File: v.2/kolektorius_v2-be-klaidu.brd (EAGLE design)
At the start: 100 x 50 mm, 81 parts, among them IC1 LM1117-33, IC2 ENC28J60, K1 G5V1, K2 G5V1, K3 G5V1, T1 2N2222, T2 2N2222, T3 2N2222, T4 2N2222, U1 ATMEGA328P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

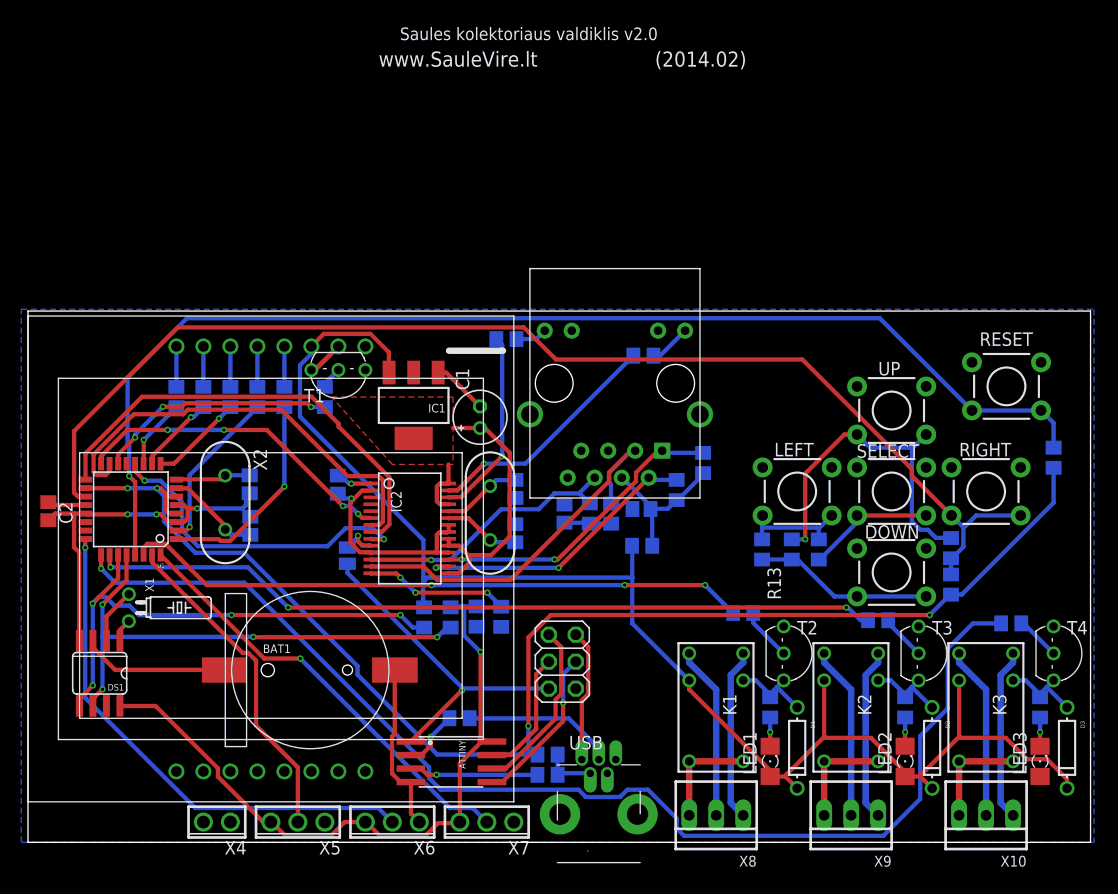
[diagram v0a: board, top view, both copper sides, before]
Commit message: prijungta prie tinklo emoncms
veikiantis pvz
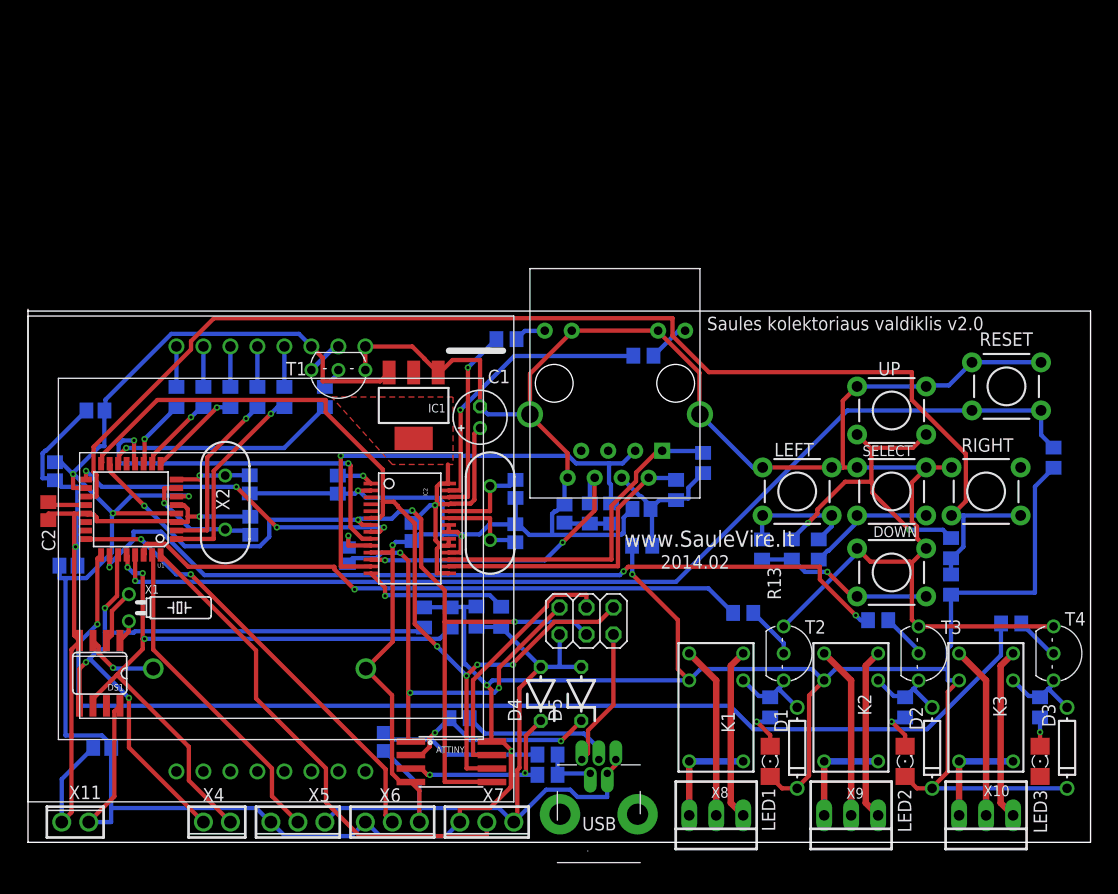
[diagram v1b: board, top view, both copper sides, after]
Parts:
- added C10, C11, C12, C14, C15, C16: 100n, resistor:C0805
- added D4, D5: (no value), diode:ZDIO-5
- added X11: (no value), con-phoenix-254:2POL254
- BAT1: device SparkFunNew:BATTCON_12MM_SMT -> SparkFun-Electromechanical:BATTCOM_20MM_PTH
- X2: value 25MHz -> 16MHz
- moved BAT1 9.23 mm to (31.8, 16.3), flipped to the bottom, turned to 0 degrees
- moved ISP 4.46 mm to (52.6, 20.8), turned to 180 degrees
- moved R14 0.05 mm to (61.0, 33.2)
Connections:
- removed net MISO: ATTINY.6, ISP.1
- removed net MOSI: ATTINY.5, ISP.4
- removed net VCC: R17.2, R9.2, RUSB.2, U1.18, U1.4, U1.6
- net +3V3: now also C14.1
- net +5V: now also C10.1, C11.2, C12.2, C15.1, C16.1, R17.2, R9.2, RUSB.2, U1.18, U1.4, U1.6, X11.2
- net D+: now also D5.C
- net D-: now also D4.C
- net D11: now also ATTINY.5, ISP.4
- net D12: now also ATTINY.6, ISP.1
- net GND: now also BAT1.2, C10.2, C11.1, C12.1, C14.2, C15.2, C16.2, D4.A, D5.A, X11.1; no longer BAT1.P$1
- net N$36: now also BAT1.1; no longer BAT1.P$2
- net SCL: now also X4.1
- net SDA: now also X4.2
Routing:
- net GND: track 77.3 -> 404.0 mm, vias 4 -> 5
- net VCC: track 128.7 -> 0.00 mm, vias 4 -> 0
- net +5V: track 204.2 -> 331.1 mm, vias 1 -> 6
- net D12: track 30.6 -> 86.3 mm
- net D11: track 41.0 -> 81.0 mm, vias 0 -> 4
- net SDA: track 48.4 -> 66.1 mm, vias 4 -> 3
- net MISO: track 16.6 -> 0.00 mm
- net SCL: track 48.7 -> 65.0 mm, vias 4 -> 3
- net MOSI: track 15.2 -> 0.00 mm, vias 1 -> 0
- net N$46: track 112.9 -> 98.4 mm
- net D+: track 5.55 -> 19.7 mm, vias 1 -> 2
- net SCK: track 12.0 -> 24.2 mm
- net N$52: track 31.3 -> 42.2 mm, vias 1 -> 3
- net D13: track 43.0 -> 32.5 mm, vias 0 -> 4
- net RD+: track 37.2 -> 45.6 mm, vias 0 -> 1
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- removed copper zone on layer 16, net GND
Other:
- board size 100 x 50 mm -> 100 x 50.2 mm
- board text added: "2014.02"
- board text removed: "(2014.02)"
